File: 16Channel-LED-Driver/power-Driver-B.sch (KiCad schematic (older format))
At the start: 17 parts, among them Q34 BC413, U6 PCA9634

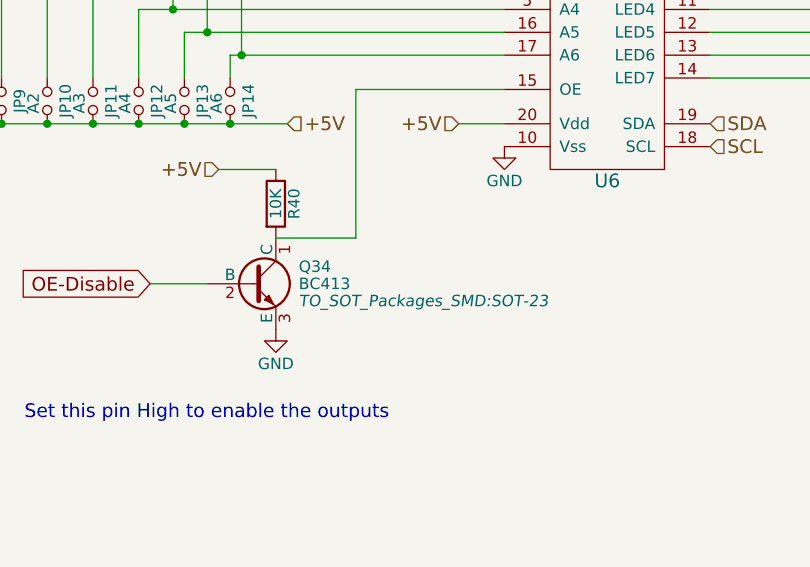
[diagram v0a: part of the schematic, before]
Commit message: Did Revision B of the 16 Channel board, also exported some gerbers
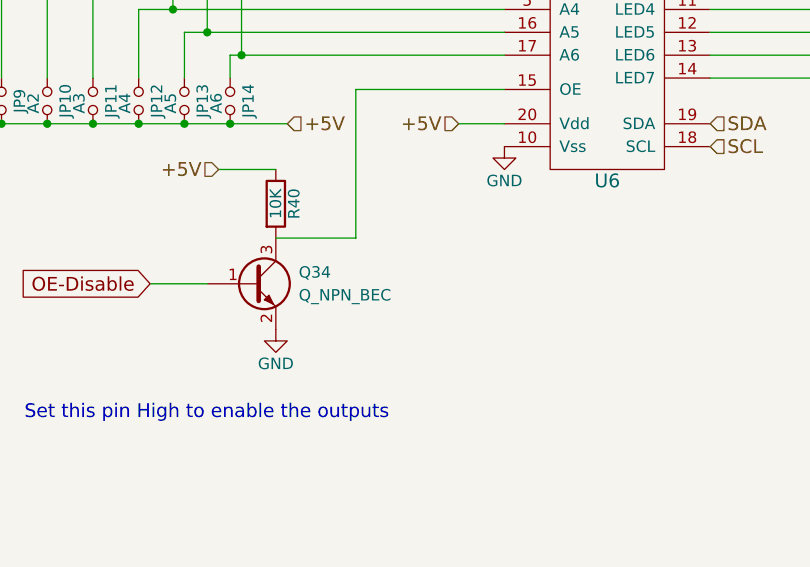
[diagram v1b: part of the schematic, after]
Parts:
- removed Q34: BC413, TO_SOT_Packages_SMD:SOT-23, symbol BC413
- added Q34: Q_NPN_BEC, TO_SOT_Packages_SMD:SOT-23, symbol Q_NPN_BEC
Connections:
- net GND: now also Q34.2 (E)
- net OE-Disable: now also Q34.1 (B)
- net at R40.2, U6.15 (OE): now also Q34.3 (C)
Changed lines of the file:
@@
 Connection ~ 2250 1150
 $Comp
-L GND #PWR048
+L GND #PWR050
 U 1 1 588C0743
 P 2500 1150
-AR Path="/588C5EEC/588C0743" Ref="#PWR048"  Part="1"
+AR Path="/588C5EEC/588C0743" Ref="#PWR050"  Part="1"
 AR Path="/588BB842/588C0743" Ref="#PWR07"  Part="1"
-F 0 "#PWR048" H 2500 900 50  0001 C CNN
+F 0 "#PWR050" H 2500 900 50  0001 C CNN
 F 1 "GND" H 2500 1000 50  0000 C CNN
 F 2 "" H 2500 1150 50  0000 C CNN
@@
 	1    0    0    -1
 $EndComp
-$Comp
-L BC413 Q34
-U 1 1 588C0745
-P 2300 3200
-AR Path="/588C5EEC/588C0745" Ref="Q34"  Part="1"
-AR Path="/588BB842/588C0745" Ref="Q1"  Part="1"
-F 0 "Q34" H 2500 3275 50  0000 L CNN
-F 1 "BC413" H 2500 3200 50  0000 L CNN
-F 2 "TO_SOT_Packages_SMD:SOT-23" H 2500 3125 50  0000 L CIN
-F 3 "" H 2300 3200 50  0000 L CNN
-	1    2300 3200
-	1    0    0    -1
-$EndComp
 Wire Wire Line
 	2400 2700 2150 2700
 $Comp
-L GND #PWR049
+L GND #PWR051
 U 1 1 588C0746
 P 2400 3400
-AR Path="/588C5EEC/588C0746" Ref="#PWR049"  Part="1"
+AR Path="/588C5EEC/588C0746" Ref="#PWR051"  Part="1"
 AR Path="/588BB842/588C0746" Ref="#PWR08"  Part="1"
-F 0 "#PWR049" H 2400 3150 50  0001 C CNN
+F 0 "#PWR051" H 2400 3150 50  0001 C CNN
 F 1 "GND" H 2400 3250 50  0000 C CNN
 F 2 "" H 2400 3400 50  0000 C CNN
@@
 +5V
 $Comp
-L GND #PWR050
+L GND #PWR052
 U 1 1 588BDC8D
 P 3400 2600
-AR Path="/588C5EEC/588BDC8D" Ref="#PWR050"  Part="1"
+AR Path="/588C5EEC/588BDC8D" Ref="#PWR052"  Part="1"
 AR Path="/588BB842/588BDC8D" Ref="#PWR09"  Part="1"
-F 0 "#PWR050" H 3400 2350 50  0001 C CNN
+F 0 "#PWR052" H 3400 2350 50  0001 C CNN
 F 1 "GND" H 3400 2450 50  0000 C CNN
 F 2 "" H 3400 2600 50  0000 C CNN
@@
 Text Notes 1300 3800 0    60   ~ 0
 Set this pin High to enable the outputs
+$Comp
+L Q_NPN_BEC Q34
+U 1 1 5976E9E0
+P 2300 3200
+F 0 "Q34" H 2500 3250 50  0000 L CNN
+F 1 "Q_NPN_BEC" H 2500 3150 50  0000 L CNN
+F 2 "TO_SOT_Packages_SMD:SOT-23" H 2500 3300 50  0001 C CNN
+F 3 "" H 2300 3200 50  0000 C CNN
+	1    2300 3200
+	1    0    0    -1
+$EndComp
 $EndSCHEMATC
